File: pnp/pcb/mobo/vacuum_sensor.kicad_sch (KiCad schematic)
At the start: 8 parts, among them U2 TL072, U3 XGZP101SB1, U6 2SMPP-03, U7 INA128

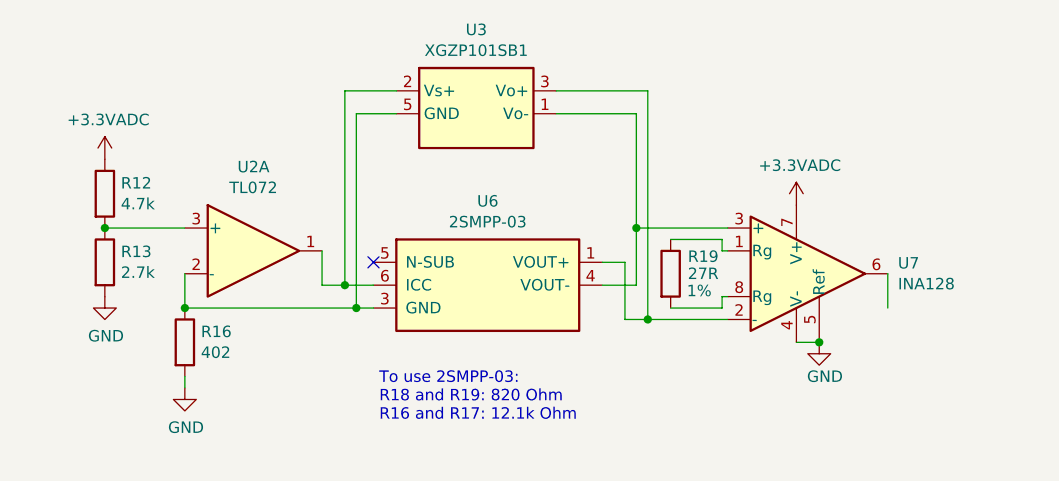
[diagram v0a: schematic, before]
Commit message: All sheets cleaned up
All symbols and their fields are now neatly organized.

All hierarchical pins are already imported,
except for the microcontroller sheet.
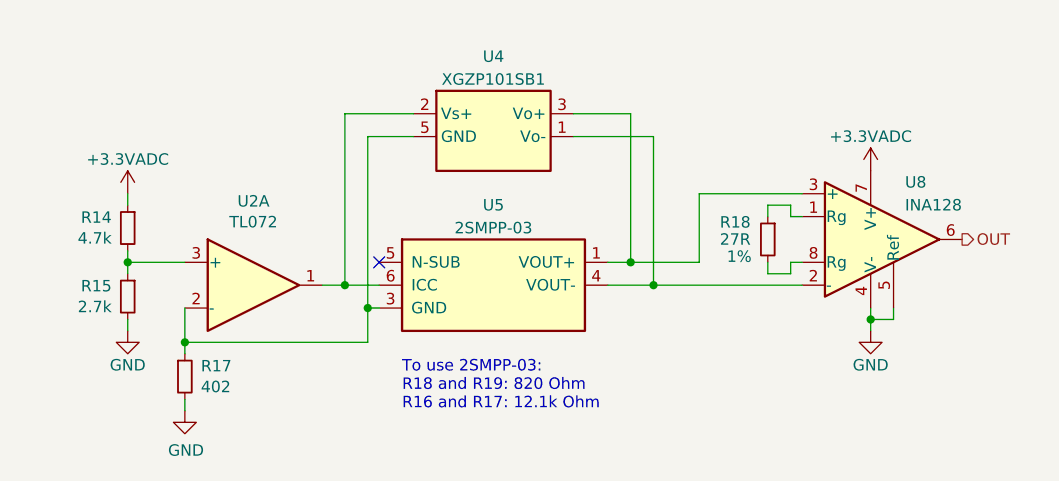
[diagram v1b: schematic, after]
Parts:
- R14: renamed from R12; symbol Device:R -> Device:R_Small
- R15: renamed from R13; symbol Device:R -> Device:R_Small
- R17: renamed from R16; symbol Device:R -> Device:R_Small
- R18: renamed from R19; symbol Device:R -> Device:R_Small
- renumbered U3 to U4, U6 to U5, U7 to U8
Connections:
- net at U4.3 (Vo+), U5.1 (VOUT+): now also U8.3 (+); no longer U8.2 (-)
- net at U4.1 (Vo-), U4.6 (Vo-), U5.4 (VOUT-): now also U8.2 (-); no longer U8.3 (+)
- net OUT: now reaches U8.6
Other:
- moved on the sheet: R14, R15, R17, R18, U2A, U4, U5, U8

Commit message: Connect all sub-sheets together
Refactored schematic is checked against existing lay-out.
Connectivity has stayed the same.
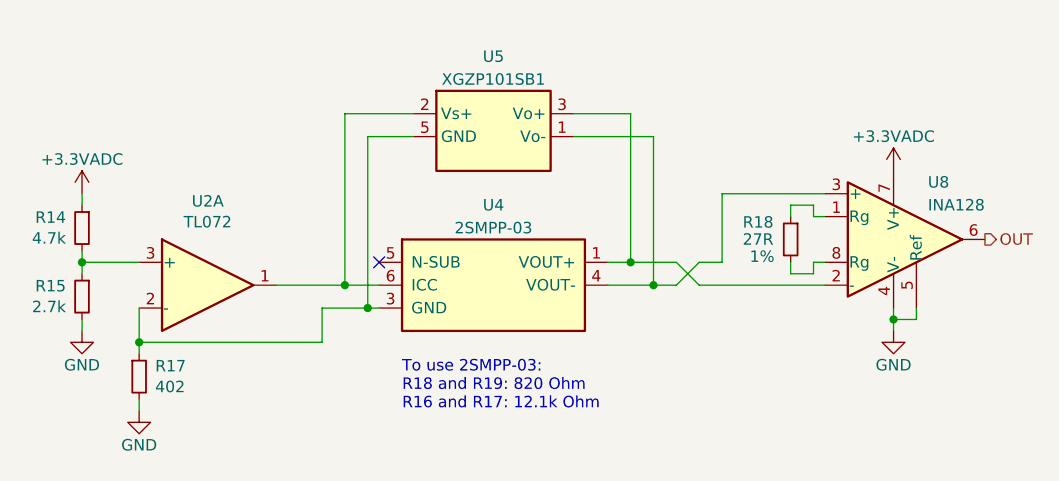
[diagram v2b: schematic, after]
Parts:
- renumbered U5 to U4, U4 to U5
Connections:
- net at U4.1 (VOUT+), U5.3 (Vo+): now also U8.2 (-); no longer U8.3 (+)
- net at U4.4 (VOUT-), U5.1 (Vo-), U5.6 (Vo-): now also U8.3 (+); no longer U8.2 (-)
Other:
- moved on the sheet: R14, R15, R17, R18, U2A, U8

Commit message: Fixed schematic parity
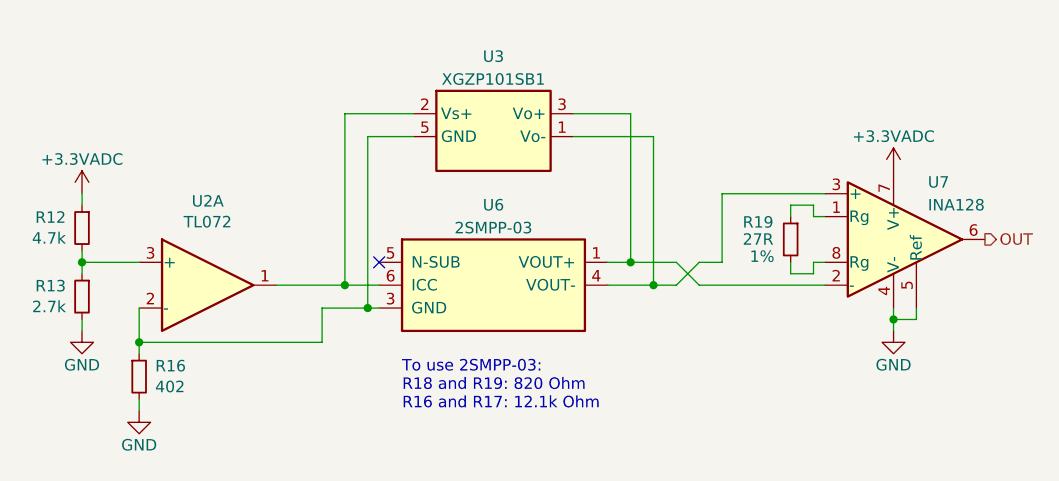
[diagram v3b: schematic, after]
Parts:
- renumbered R14 to R12, R15 to R13, R17 to R16, R18 to R19, U5 to U3, U4 to U6, U8 to U7
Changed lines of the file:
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@@
     (effects (font (size 1.27 1.27)) (justify left))
   )
-  (symbol (lib_id "power:GND") (at 96.52 114.3 0)
-    (in_bom yes) (on_board yes)
-    (property "Reference" "#PWR0240" (id 0) (at 96.52 120.65 0)
+  (symbol (lib_id "power:GND") (at 96.52 114.3 0) (unit 1)
+    (in_bom yes) (on_board yes)
+    (property "Reference" "#PWR0100" (id 0) (at 96.52 120.65 0)
       (effects (font (size 1.27 1.27)) hide)
     )
@@
     (pin "1")
   )
-  (symbol (lib_id "power:+3.3VADC") (at 96.52 99.06 0)
-    (in_bom yes) (on_board yes)
-    (property "Reference" "#PWR0241" (id 0) (at 100.33 100.33 0)
+  (symbol (lib_id "power:+3.3VADC") (at 96.52 99.06 0) (unit 1)
+    (in_bom yes) (on_board yes)
+    (property "Reference" "#PWR099" (id 0) (at 100.33 100.33 0)
       (effects (font (size 1.27 1.27)) hide)
     )
@@
     (pin "1")
   )
-  (symbol (lib_id "Device:R_Small") (at 102.87 119.38 0)
-    (in_bom yes) (on_board yes)
-    (property "Reference" "R17" (id 0) (at 104.648 118.2116 0)
+  (symbol (lib_id "Device:R_Small") (at 102.87 119.38 0) (unit 1)
+    (in_bom yes) (on_board yes)
+    (property "Reference" "R16" (id 0) (at 104.648 118.2116 0)
       (effects (font (size 1.27 1.27)) (justify left))
     )
@@
     (pin "2")
   )
-  (symbol (lib_id "index:2SMPP-03") (at 142.24 109.22 0)
-    (in_bom yes) (on_board yes)
-    (property "Reference" "U4" (id 0) (at 142.24 100.33 0))
+  (symbol (lib_id "index:2SMPP-03") (at 142.24 109.22 0) (unit 1)
+    (in_bom yes) (on_board yes)
+    (property "Reference" "U6" (id 0) (at 142.24 100.33 0))
     (property "Value" "2SMPP-03" (id 1) (at 142.24 102.87 0))
     (property "Footprint" "index:2SMPP-03" (id 2) (at 140.97 115.57 0)
@@
     (pin "6")
   )
-  (symbol (lib_id "Device:R_Small") (at 96.52 110.49 0) (mirror y)
-    (in_bom yes) (on_board yes)
-    (property "Reference" "R15" (id 0) (at 94.742 109.3216 0)
+  (symbol (lib_id "Device:R_Small") (at 96.52 110.49 0) (mirror y) (unit 1)
+    (in_bom yes) (on_board yes)
+    (property "Reference" "R13" (id 0) (at 94.742 109.3216 0)
       (effects (font (size 1.27 1.27)) (justify left))
     )
@@
     (pin "2")
   )
-  (symbol (lib_id "Device:R_Small") (at 175.26 104.14 0) (mirror y)
-    (in_bom yes) (on_board yes)
-    (property "Reference" "R18" (id 0) (at 173.355 102.235 0)
+  (symbol (lib_id "Device:R_Small") (at 175.26 104.14 0) (mirror y) (unit 1)
+    (in_bom yes) (on_board yes)
+    (property "Reference" "R19" (id 0) (at 173.355 102.235 0)
       (effects (font (size 1.27 1.27)) (justify left))
     )
@@
     (pin "2")
   )
-  (symbol (lib_id "index:XGZP") (at 142.24 92.71 0)
-    (in_bom yes) (on_board yes)
-    (property "Reference" "U5" (id 0) (at 142.24 83.82 0))
+  (symbol (lib_id "index:XGZP") (at 142.24 92.71 0) (unit 1)
+    (in_bom yes) (on_board yes)
+    (property "Reference" "U3" (id 0) (at 142.24 83.82 0))
     (property "Value" "XGZP101SB1" (id 1) (at 142.24 86.36 0))
     (property "Footprint" "index:SO-6_7x7mm_P2.54mm" (id 2) (at 142.24 105.41 0)
@@
     (pin "6")
   )
-  (symbol (lib_id "power:GND") (at 102.87 123.19 0)
-    (in_bom yes) (on_board yes)
-    (property "Reference" "#PWR0239" (id 0) (at 102.87 129.54 0)
+  (symbol (lib_id "power:GND") (at 102.87 123.19 0) (unit 1)
+    (in_bom yes) (on_board yes)
+    (property "Reference" "#PWR0103" (id 0) (at 102.87 129.54 0)
       (effects (font (size 1.27 1.27)) hide)
     )
@@
     (pin "1")
   )
-  (symbol (lib_id "Amplifier_Operational:TL072") (at 110.49 109.22 0)
+  (symbol (lib_id "Amplifier_Operational:TL072") (at 110.49 109.22 0) (unit 1)
     (in_bom yes) (on_board yes)
     (property "Reference" "U2" (id 0) (at 110.49 99.8982 0))
@@
       (effects (font (size 1.27 1.27)) hide)
     )
+    (pin "1")
+    (pin "2")
+    (pin "3")
     (pin "5")
     (pin "6")
     (pin "7")
-  )
-  (symbol (lib_id "Device:R_Small") (at 96.52 102.87 0) (mirror y)
-    (in_bom yes) (on_board yes)
-    (property "Reference" "R14" (id 0) (at 94.742 101.7016 0)
+    (pin "4")
+    (pin "8")
+  )
+  (symbol (lib_id "Device:R_Small") (at 96.52 102.87 0) (mirror y) (unit 1)
+    (in_bom yes) (on_board yes)
+    (property "Reference" "R12" (id 0) (at 94.742 101.7016 0)
       (effects (font (size 1.27 1.27)) (justify left))
     )
@@
     (pin "2")
   )
-  (symbol (lib_id "power:+3.3VADC") (at 186.69 96.52 0)
-    (in_bom yes) (on_board yes)
-    (property "Reference" "#PWR0242" (id 0) (at 190.5 97.79 0)
+  (symbol (lib_id "power:+3.3VADC") (at 186.69 96.52 0) (unit 1)
+    (in_bom yes) (on_board yes)
+    (property "Reference" "#PWR0105" (id 0) (at 190.5 97.79 0)
       (effects (font (size 1.27 1.27)) hide)
     )
@@
     (pin "1")
   )
-  (symbol (lib_id "power:GND") (at 186.69 114.3 0)
-    (in_bom yes) (on_board yes)
-    (property "Reference" "#PWR0243" (id 0) (at 186.69 120.65 0)
+  (symbol (lib_id "power:GND") (at 186.69 114.3 0) (unit 1)
+    (in_bom yes) (on_board yes)
+    (property "Reference" "#PWR0107" (id 0) (at 186.69 120.65 0)
       (effects (font (size 1.27 1.27)) hide)
     )
@@
     (pin "1")
   )
-  (symbol (lib_id "Amplifier_Instrumentation:INA128") (at 186.69 104.14 0)
-    (in_bom yes) (on_board yes)
-    (property "Reference" "U8" (id 0) (at 190.5 97.79 0)
-      (effects (font (size 1.27 1.27)) (justify left))
-    )
+  (symbol (lib_id "Amplifier_Instrumentation:INA128") (at 186.69 104.14 0) (unit 1)
+    (in_bom yes) (on_board yes)
+    (property "Reference" "U7" (id 0) (at 190.5 97.79 0)
+      (effects (font (size 1.27 1.27)) (justify left))
+    )

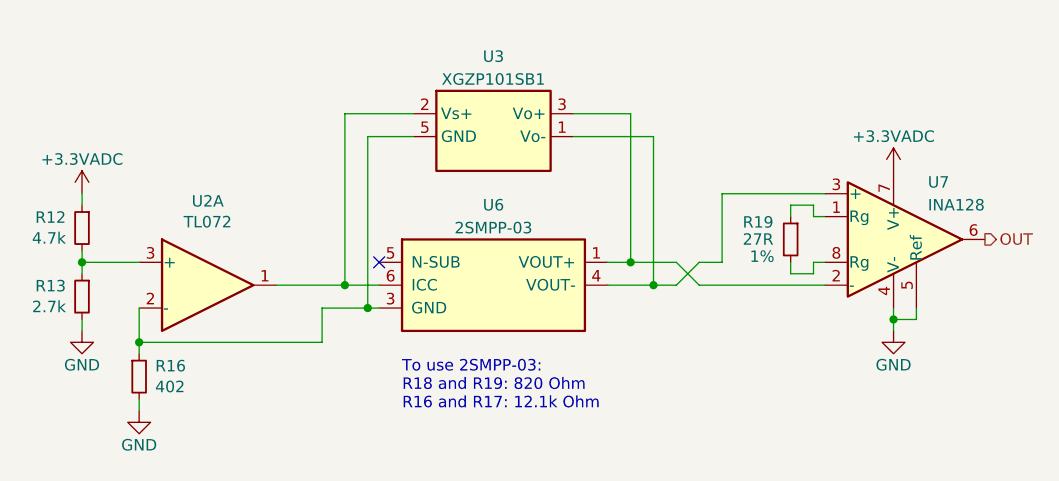
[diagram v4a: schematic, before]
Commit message: moving mobo-rev04b0 into mobo-rev04 branch from old repo
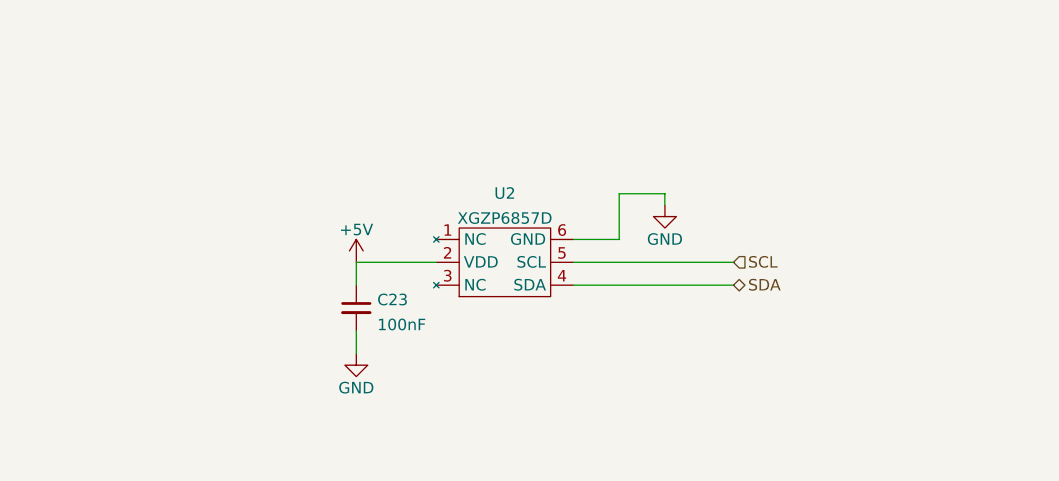
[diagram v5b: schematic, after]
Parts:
- removed R12: 4.7k, Resistor_SMD:R_0805_2012Metric, symbol Device:R_Small
- removed R13: 2.7k, Resistor_SMD:R_0805_2012Metric, symbol Device:R_Small
- removed R16: 402, Resistor_SMD:R_0805_2012Metric, symbol Device:R_Small
- removed R19: 27R, Resistor_SMD:R_0805_2012Metric, symbol Device:R_Small
- removed U2: TL072, Package_SO:SOIC-8_3.9x4.9mm_P1.27mm, symbol Amplifier_Operational:TL072
- removed U3: XGZP101SB1, index:SO-6_7x7mm_P2.54mm, symbol index:XGZP
- removed U6: 2SMPP-03, index:2SMPP-03, symbol index:2SMPP-03
- removed U7: INA128, Package_SO:SOIC-8_3.9x4.9mm_P1.27mm, symbol Amplifier_Instrumentation:INA128
- added C23: 100nF, Capacitor_SMD:C_0805_2012Metric, symbol Device:C_Small
- added U2: XGZP6857D, index:XGZP6857D, symbol index:XGZP6857D
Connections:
- net GND: now also C23.2, U2.6 (GND)
- new net +5V: C23.1, U2.2 (VDD)
- new net SCL: U2.5 (SCL)
- new net SDA: U2.4 (SDA)
- no-connect marks 1 -> 0
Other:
- note removed: "To use 2SMPP-03: R18 and R19: 820 Ohm R16 and R17: 12.1k Ohm"
